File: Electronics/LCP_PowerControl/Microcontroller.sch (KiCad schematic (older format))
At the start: 21 parts, among them J5 Conn_02x05_Odd_Even, SW1 SW_Push, U3 MSP430FR5989, Y1 32.768kHz

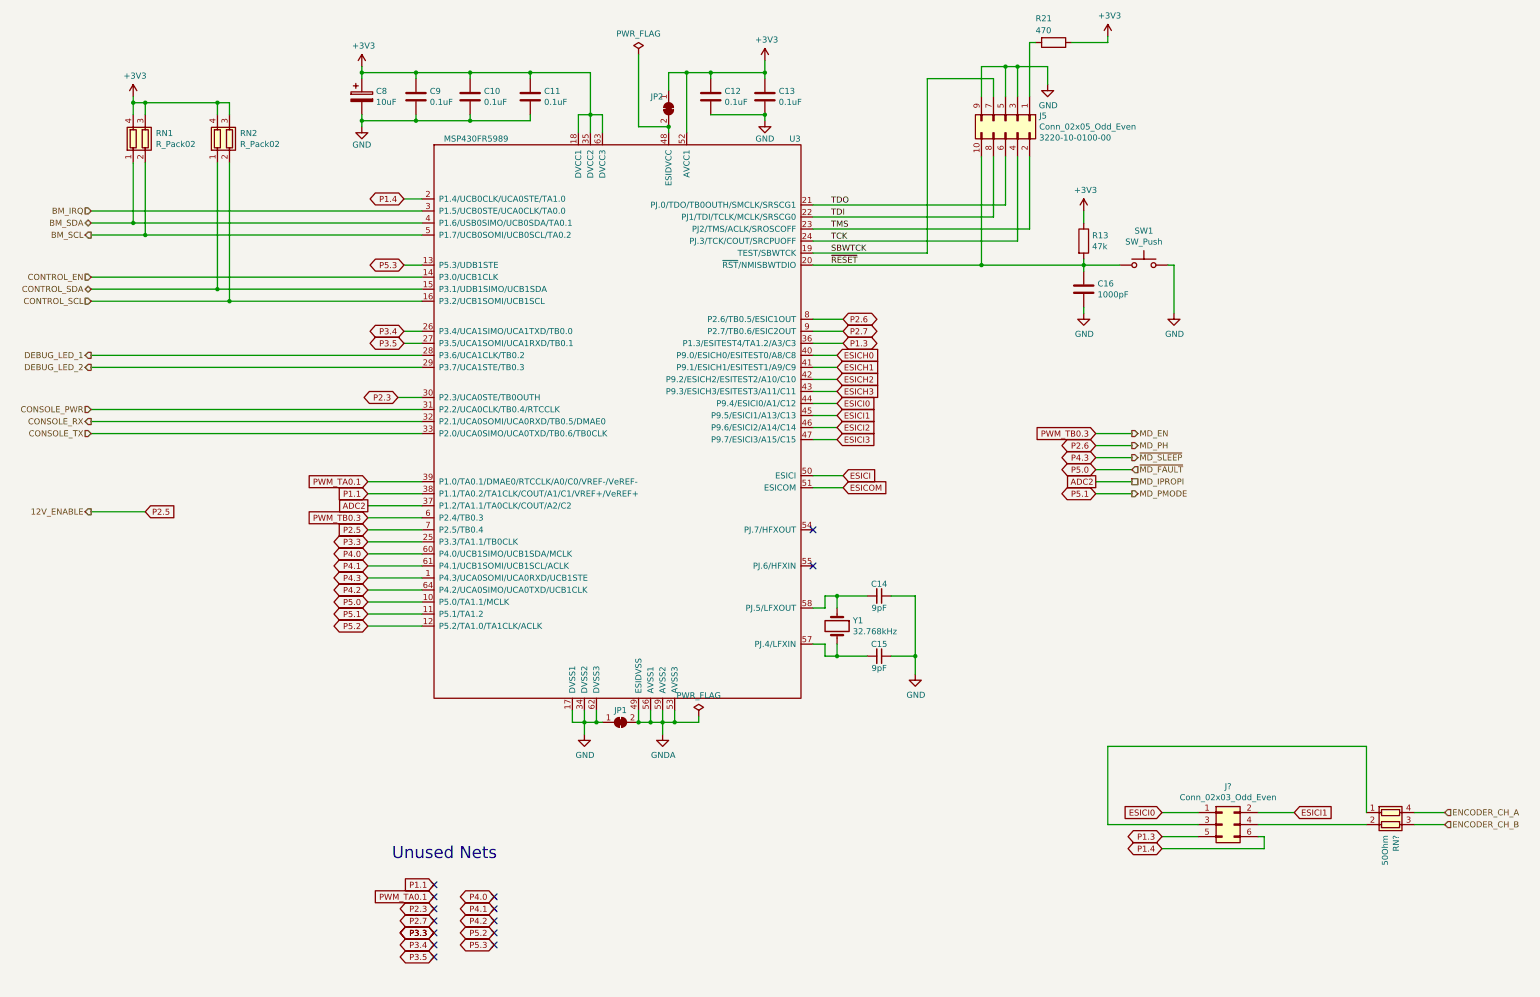
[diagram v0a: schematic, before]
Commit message: adding power control to pull-ups.
Adding ability to power on/off the pull-ups on the encoder
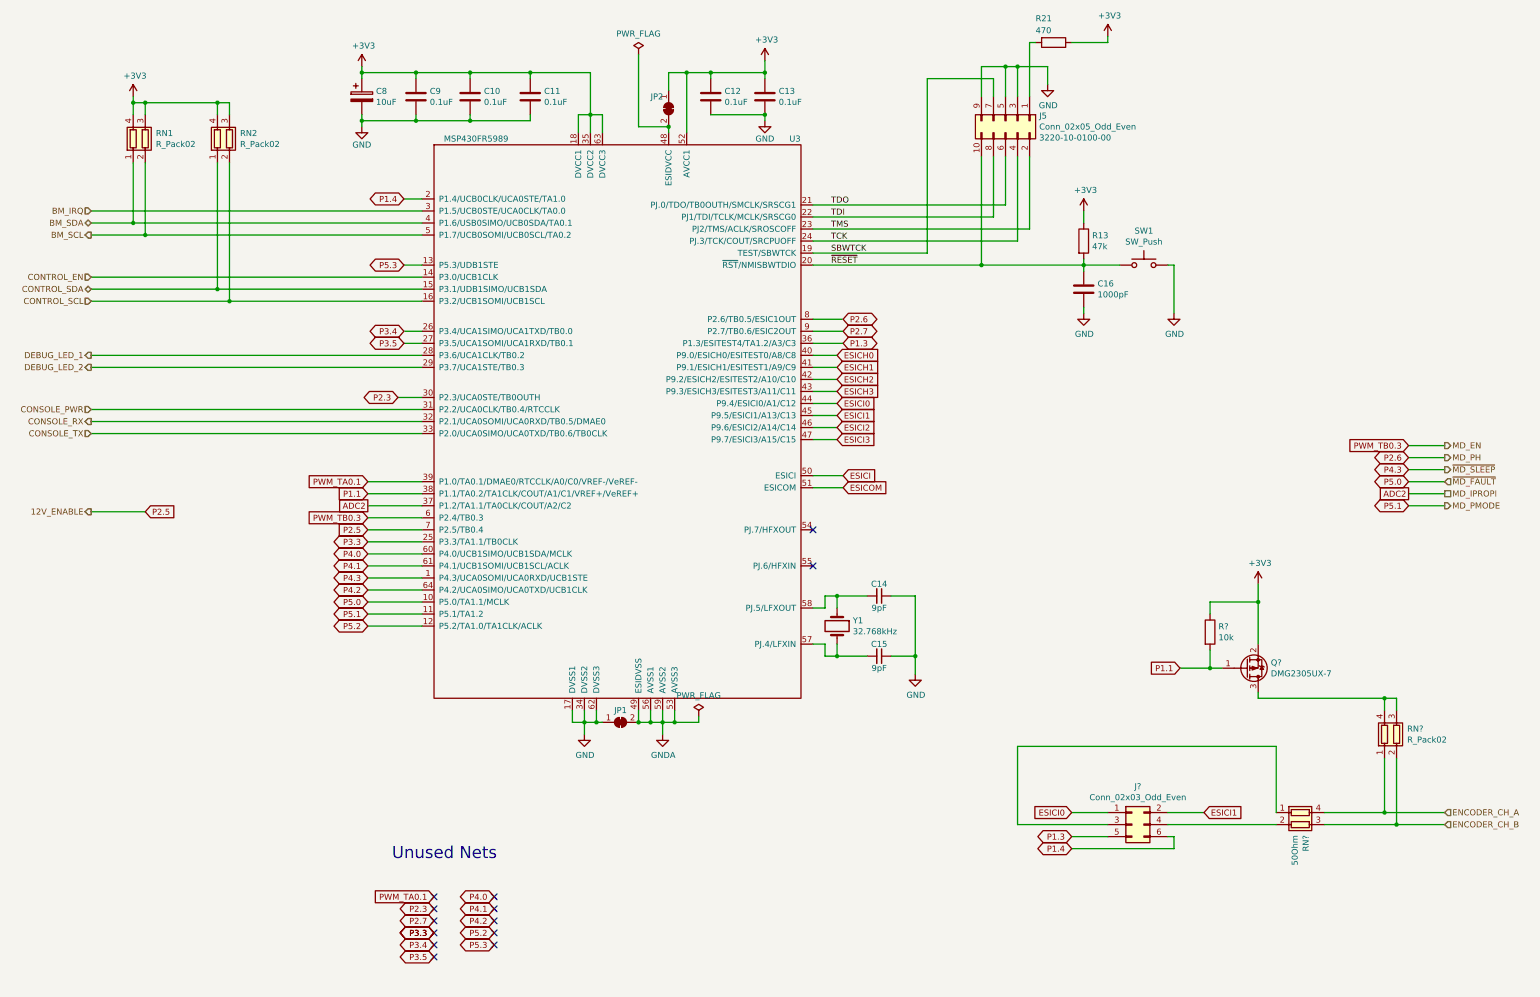
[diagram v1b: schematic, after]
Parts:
- added Q?: DMG2305UX-7, Package_TO_SOT_SMD:SOT-23, symbol Transistor_FET:DMG2301L
- added R?: 10k, Resistor_SMD:R_0805_2012Metric, symbol Device:R
- added RN?: R_Pack02, Resistor_SMD:R_Array_Concave_2x0603, symbol Device:R_Pack02
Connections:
- net +3V3: now also Q?.2 (S), R?.1
- net ENCODER_CH_A: now also RN?.1 (R1.1)
- net ENCODER_CH_B: now also RN?.2 (R2.1)
- net P1.1: now also Q?.1 (G), R?.2
- new net: Q?.3 (D), RN?.3 (R2.2), RN?.4 (R1.2)
- no-connect marks 14 -> 13
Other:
- moved on the sheet: J?, RN?
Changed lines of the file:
@@
 Text HLabel 3900 4800 0    50   Output ~ 0
 CONSOLE_RX
-Text HLabel 12550 4900 2    50   Output ~ 0
+Text HLabel 15150 5000 2    50   Output ~ 0
 MD_EN
-Text HLabel 12550 5000 2    50   Output ~ 0
+Text HLabel 15150 5100 2    50   Output ~ 0
 MD_PH
-Text HLabel 12550 5200 2    50   Input ~ 0
+Text HLabel 15150 5300 2    50   Input ~ 0
 ~MD_FAULT
-Text HLabel 12550 5300 2    50   UnSpc ~ 0
+Text HLabel 15150 5400 2    50   UnSpc ~ 0
 MD_IPROPI
-Text HLabel 12550 5400 2    50   Output ~ 0
+Text HLabel 15150 5500 2    50   Output ~ 0
 MD_PMODE
-Text HLabel 12550 5100 2    50   Output ~ 0
+Text HLabel 15150 5200 2    50   Output ~ 0
 ~MD_SLEEP
 Text HLabel 3900 5550 0    50   Output ~ 0
@@
 P4.2
 Wire Wire Line
-	12250 5000 12550 5000
-Text GLabel 12250 5100 0    50   BiDi ~ 0
+	14850 5100 15150 5100
+Text GLabel 14850 5200 0    50   BiDi ~ 0
 P4.3
 Wire Wire Line
-	12250 5100 12550 5100
-Text GLabel 12250 5200 0    50   BiDi ~ 0
+	14850 5200 15150 5200
+Text GLabel 14850 5300 0    50   BiDi ~ 0
 P5.0
 Wire Wire Line
-	12250 5200 12550 5200
+	14850 5300 15150 5300
 Text GLabel 6200 5500 0    50   UnSpc ~ 0
 ADC2
 Wire Wire Line
 	6200 5500 6650 5500
-Text GLabel 12250 4900 0    50   Input ~ 0
+Text GLabel 14850 5000 0    50   Input ~ 0
 PWM_TB0.3
-Text GLabel 12250 5300 0    50   UnSpc ~ 0
+Text GLabel 14850 5400 0    50   UnSpc ~ 0
 ADC2
 Wire Wire Line
-	12250 5300 12550 5300
-Text GLabel 12250 5400 0    50   BiDi ~ 0
+	14850 5400 15150 5400
+Text GLabel 14850 5500 0    50   BiDi ~ 0
 P5.1
 Wire Wire Line
-	12250 5400 12550 5400
+	14850 5500 15150 5500
 Text HLabel 15150 8050 2    50   Input ~ 0
 ENCODER_CH_A
 Text HLabel 15150 8150 2    50   Input ~ 0
 ENCODER_CH_B
-Text GLabel 12800 8050 0    50   Input ~ 0
+Text GLabel 12050 8050 0    50   Input ~ 0
 ESICI0
-Text GLabel 13900 8050 2    50   Input ~ 0
+Text GLabel 13150 8050 2    50   Input ~ 0
 ESICI1
 Text GLabel 4350 5550 2    50   Input ~ 0
@@
 Text GLabel 7250 9150 0    50   BiDi ~ 0
 P5.3
-Text GLabel 12800 8350 0    50   BiDi ~ 0
+Text GLabel 12050 8350 0    50   BiDi ~ 0
 P1.4
 Text GLabel 10150 3950 2    50   BiDi ~ 0
@@
 Wire Wire Line
 	10150 3950 9900 3950
-Text GLabel 12250 5000 0    50   BiDi ~ 0
+Text GLabel 14850 5100 0    50   BiDi ~ 0
 P2.6
 Text GLabel 6750 8950 0    50   BiDi ~ 0
 P2.7
-Text GLabel 12800 8250 0    50   BiDi ~ 0
+Text GLabel 12050 8250 0    50   BiDi ~ 0
 P1.3
 Text GLabel 6450 4600 0    50   BiDi ~ 0
@@
 Connection ~ 4250 3150
 Wire Wire Line
-	12250 4900 12550 4900
+	14850 5000 15150 5000
 Text HLabel 3900 4700 0    50   Input ~ 0
 CONSOLE_PWR
@@
 Text GLabel 6750 9050 0    50   BiDi ~ 0
 P3.3
-Text GLabel 6750 8650 0    50   Input ~ 0
+Text GLabel 12950 6850 0    50   Input ~ 0
 P1.1
-NoConn ~ 6750 8650
 Text GLabel 6750 9150 0    50   BiDi ~ 0
 P3.4
@@
 L Connector_Generic:Conn_02x03_Odd_Even J?
 U 1 1 60479EE2
-P 13300 8150
-F 0 "J?" H 13350 8467 50  0000 C CNN
-F 1 "Conn_02x03_Odd_Even" H 13350 8376 50  0000 C CNN
-F 2 "Connector_PinHeader_2.54mm:PinHeader_2x03_P2.54mm_Vertical" H 13300 8150 50  0001 C CNN
-F 3 "~" H 13300 8150 50  0001 C CNN
-	1    13300 8150
-	1    0    0    -1
-$EndComp
-Wire Wire Line
-	12800 8050 13100 8050
-Wire Wire Line
-	13900 8050 13600 8050
+P 12550 8150
+F 0 "J?" H 12600 8467 50  0000 C CNN
+F 1 "Conn_02x03_Odd_Even" H 12600 8376 50  0000 C CNN
+F 2 "Connector_PinHeader_2.54mm:PinHeader_2x03_P2.54mm_Vertical" H 12550 8150 50  0001 C CNN
+F 3 "~" H 12550 8150 50  0001 C CNN
+	1    12550 8150
+	1    0    0    -1
+$EndComp
+Wire Wire Line
+	12050 8050 12350 8050
+Wire Wire Line
+	13150 8050 12850 8050
 $Comp
 L Device:R_Pack02 RN?
 U 1 1 604C7193
-P 14700 8150
-F 0 "RN?" H 14788 8196 50  0000 L CNN
-F 1 "50Ohm" H 14788 8105 50  0000 L CNN
-F 2 "Resistor_SMD:R_Array_Concave_2x0603" V 14875 8150 50  0001 C CNN
-F 3 "~" H 14700 8150 50  0001 C CNN
-F 4 "EXB-V4V510JV" H 14700 8150 50  0001 C CNN "MPN"
-	1    14700 8150
+P 13950 8150
+F 0 "RN?" H 14038 8196 50  0000 L CNN
+F 1 "50Ohm" H 14038 8105 50  0000 L CNN
+F 2 "Resistor_SMD:R_Array_Concave_2x0603" V 14125 8150 50  0001 C CNN
+F 3 "~" H 13950 8150 50  0001 C CNN
+F 4 "EXB-V4V510JV" H 13950 8150 50  0001 C CNN "MPN"
+	1    13950 8150
 	0    1    1    0
 $EndComp
 Wire Wire Line
-	13100 8250 12800 8250
-Wire Wire Line
-	12800 8350 13650 8350
-Wire Wire Line
-	13650 8350 13650 8250
-Wire Wire Line
-	13650 8250 13600 8250
-Wire Wire Line
-	14500 8150 13600 8150
-Wire Wire Line
-	14500 8050 14500 7500
-Wire Wire Line
-	14500 7500 12350 7500
-Wire Wire Line
-	12350 7500 12350 8150
-Wire Wire Line
-	12350 8150 13100 8150
-Wire Wire Line
-	15150 8150 14900 8150
-Wire Wire Line
-	15150 8050 14900 8050
+	12350 8250 12050 8250
+Wire Wire Line
+	12050 8350 12900 8350
+Wire Wire Line
+	12900 8350 12900 8250
+Wire Wire Line
+	12900 8250 12850 8250
+Wire Wire Line
+	13750 8150 12850 8150
+Wire Wire Line
+	13750 8050 13750 7500
+Wire Wire Line
+	13750 7500 11600 7500
+Wire Wire Line
+	11600 7500 11600 8150
+Wire Wire Line
+	11600 8150 12350 8150
+$Comp
+L Transistor_FET:DMG2301L Q?
+U 1 1 604912AC
+P 13500 6850
+F 0 "Q?" H 13705 6804 50  0000 L CNN
+F 1 "DMG2305UX-7" H 13705 6895 50  0000 L CNN
+F 2 "Package_TO_SOT_SMD:SOT-23" H 13700 6775 50  0001 L CIN
+F 3 "https://www.diodes.com/assets/Datasheets/DMG2305UX.pdf" H 13500 6850 50  0001 L CNN
+	1    13500 6850
+	1    0    0    1
+$EndComp
+Wire Wire Line
+	14150 8050 14650 8050
+Wire Wire Line
+	14150 8150 14750 8150
+Wire Wire Line
+	13300 6850 13200 6850
+$Comp
+L Device:R_Pack02 RN?
+U 1 1 604F4633
+P 14750 7400
+AR Path="/5EE2A5A7/604F4633" Ref="RN?"  Part="1"
+AR Path="/5EE7B8CC/604F4633" Ref="RN?"  Part="1"
+F 0 "RN?" H 14838 7446 50  0000 L CNN
+F 1 "R_Pack02" H 14838 7355 50  0000 L CNN
+F 2 "Resistor_SMD:R_Array_Concave_2x0603" V 14925 7400 50  0001 C CNN
+F 3 "~" H 14750 7400 50  0001 C CNN
+F 4 "EXB-V4V472JV" H 14750 7400 50  0001 C CNN "MPN"
+	1    14750 7400
+	1    0    0    -1
+$EndComp
+Wire Wire Line
+	14750 7200 14750 7100
+Wire Wire Line
+	14750 7100 14650 7100
+Connection ~ 14650 7100
+Wire Wire Line
+	14650 7100 14650 7200
+$Comp
+L power:+3V3 #PWR?
+U 1 1 604F4639
+P 13600 6150
+AR Path="/5EE2A5A7/604F4639" Ref="#PWR?"  Part="1"
+AR Path="/5EE7B8CC/604F4639" Ref="#PWR?"  Part="1"
+F 0 "#PWR?" H 13600 6000 50  0001 C CNN
+F 1 "+3V3" H 13615 6323 50  0000 C CNN
+F 2 "" H 13600 6150 50  0001 C CNN
+F 3 "" H 13600 6150 50  0001 C CNN
+	1    13600 6150
+	1    0    0    -1
+$EndComp
+Wire Wire Line
+	13600 7050 13600 7100
+Wire Wire Line
+	13600 7100 14650 7100
+$Comp
+L Device:R R?
+U 1 1 605237E3
+P 13200 6550
+AR Path="/5EE2AB43/605237E3" Ref="R?"  Part="1"
+AR Path="/5EE2A5A7/605237E3" Ref="R?"  Part="1"
+F 0 "R?" H 13270 6596 50  0000 L CNN
+F 1 "10k" H 13270 6505 50  0000 L CNN
+F 2 "Resistor_SMD:R_0805_2012Metric" V 13130 6550 50  0001 C CNN
+F 3 "~" H 13200 6550 50  0001 C CNN
+F 4 "RNCP0805FTD10K0" H 13200 6550 50  0001 C CNN "MPN"
+	1    13200 6550
+	1    0    0    -1
+$EndComp
+Wire Wire Line
+	13600 6150 13600 6300
+Wire Wire Line
+	13600 6300 13200 6300
+Wire Wire Line
+	13200 6300 13200 6400
+Connection ~ 13600 6300
+Wire Wire Line
+	13600 6300 13600 6650
+Connection ~ 13200 6850
+Wire Wire Line
+	13200 6850 12950 6850
+Wire Wire Line
+	13200 6700 13200 6850
+Wire Wire Line
+	14650 7600 14650 8050
+Connection ~ 14650 8050
+Wire Wire Line
+	14650 8050 15150 8050
+Wire Wire Line
+	14750 7600 14750 8150
+Connection ~ 14750 8150
+Wire Wire Line
+	14750 8150 15150 8150
 $EndSCHEMATC
